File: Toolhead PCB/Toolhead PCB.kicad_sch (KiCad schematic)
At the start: 9 parts, among them J1 PicoA, J2 PicoB, J3 PicoC, J4 Heater, J5 Therm., J6 Heatbreak, J7 Part, J8 IR/ADXL, J9 µProbe

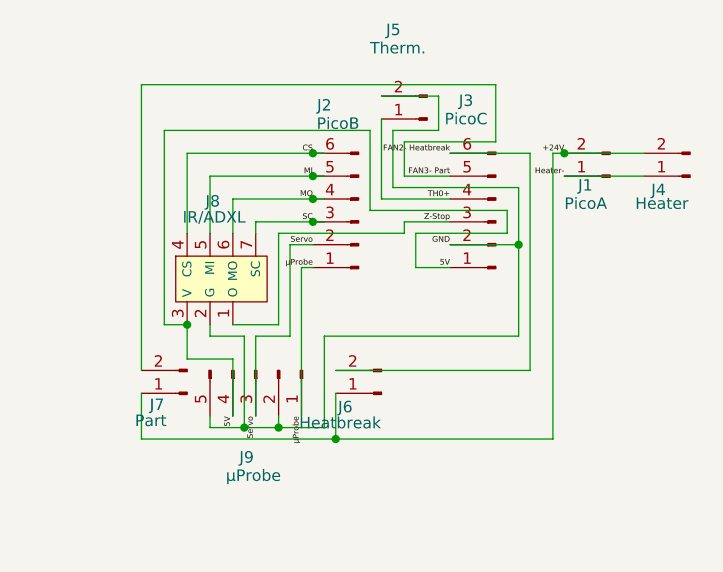
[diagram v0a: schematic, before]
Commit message: Changed Silkscreen labels.
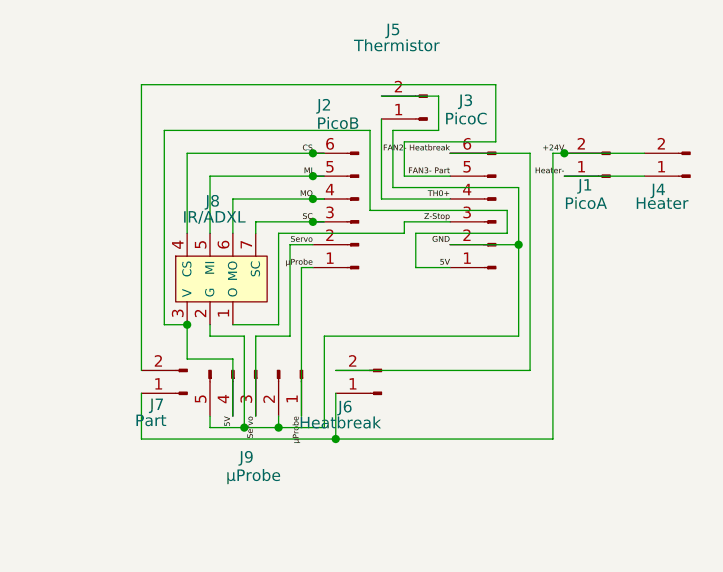
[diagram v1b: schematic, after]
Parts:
- J5: value Therm. -> Thermistor
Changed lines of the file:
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@@
 			)
 		)
-		(property "Value" "Therm."
-			(at 154.94 96.266 0)
+		(property "Value" "Thermistor"
+			(at 153.162 96.012 0)
 			(effects
 				(font

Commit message: Schematic more closely matches traces. Updated PicoB and PicoC wiring harnesses: flagged as non populated and deleted silkscreen. Removed pins from Muon 3D IR Bed Probe with ADXL345. Moved traces from PicoB to IR/ADXL so they might be easier to mill.
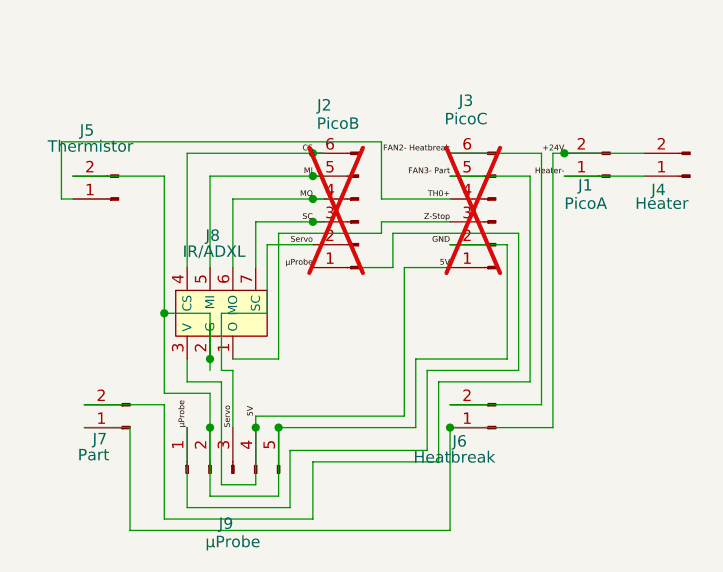
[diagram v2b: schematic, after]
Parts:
- J2, J3: now not fitted
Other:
- moved on the sheet: J5, J6, J7, J8, J9

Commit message: The 0.75mm holes do not retain the Silicone 28AWG Ribbon Cable wires properly, so the Schematic and PCB use a new footprint `SolderWire-0.1sqmm_1x06_P2.0mm_D0.4mm_OD1mm.kicad_mod` which has the same pitch and pads as the JST PH but the holes 0.75mm → 0.5mm.
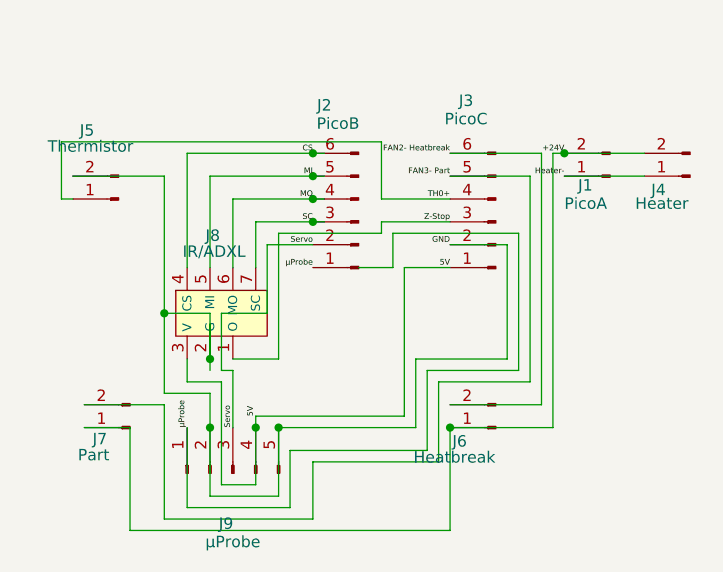
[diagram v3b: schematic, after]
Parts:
- J2, J3: footprint Connector_JST:JST_PH_B6B-PH-K_1x06_P2.00mm_Vertical -> Positron V3:SolderWire-0.1sqmm_1x06_P2.0mm_D0.4mm_OD1mm; now fitted
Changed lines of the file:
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@@
 		(in_bom yes)
 		(on_board yes)
-		(dnp yes)
+		(dnp no)
 		(property "Reference" "J2"
 			(at 149.86 102.616 0)
@@
 			)
 		)
-		(property "Footprint" "Connector_JST:JST_PH_B6B-PH-K_1x06_P2.00mm_Vertical"
+		(property "Footprint" "Positron V3:SolderWire-0.1sqmm_1x06_P2.0mm_D0.4mm_OD1mm"
 			(at 153.67 115.57 0)
 			(effects
@@
 		(in_bom yes)
 		(on_board yes)
-		(dnp yes)
+		(dnp no)
 		(property "Reference" "J3"
 			(at 165.608 102.108 0)
@@
 			)
 		)
-		(property "Footprint" "Connector_JST:JST_PH_B6B-PH-K_1x06_P2.00mm_Vertical"
+		(property "Footprint" "Positron V3:SolderWire-0.1sqmm_1x06_P2.0mm_D0.4mm_OD1mm"
 			(at 168.91 115.57 0)
 			(effects

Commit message: [2025-10-03] Moved most power traces to the back so I they could be wider while the board got narrower on the right side.
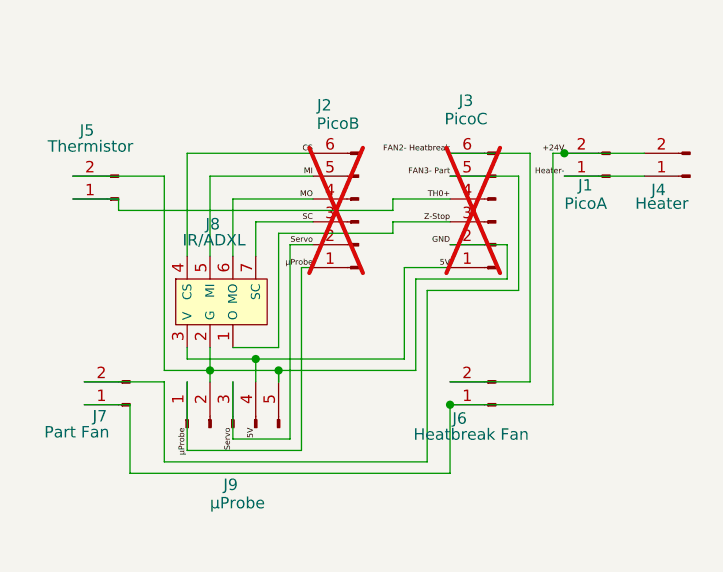
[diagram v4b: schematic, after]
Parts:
- J2, J3: footprint Positron V3:SolderWire-0.1sqmm_1x06_P2.0mm_D0.4mm_OD1mm -> Connector_JST:JST_PH_B6B-PH-K_1x06_P2.00mm_Vertical; now not fitted
- J6: value Heatbreak -> Heatbreak Fan
- J7: value Part -> Part Fan
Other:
- moved on the sheet: J6, J7, J8, J9
